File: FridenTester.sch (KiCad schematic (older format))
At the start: 16 parts, among them P1 CONN_02X05, U1 2EDN752, U2 2EDN752, U3 DG403

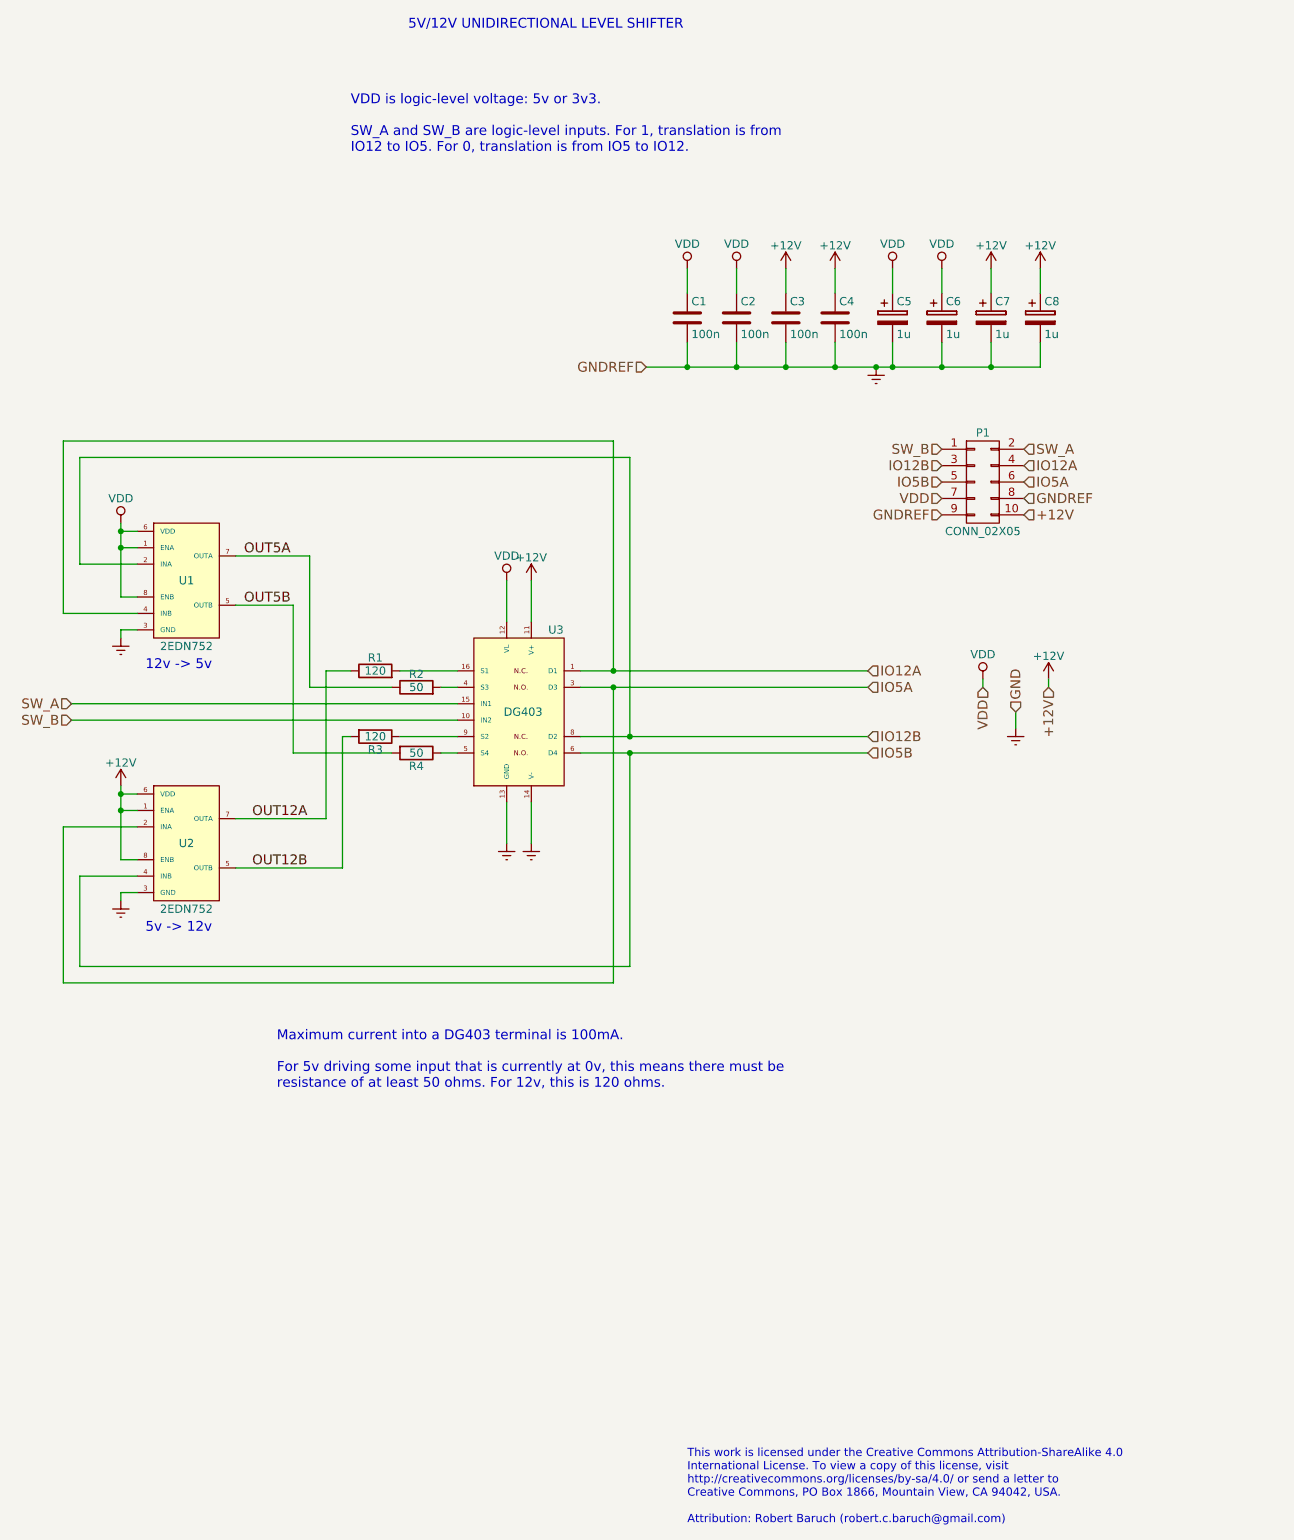
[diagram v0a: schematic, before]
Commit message: Start on rev D, with protection Schottkys
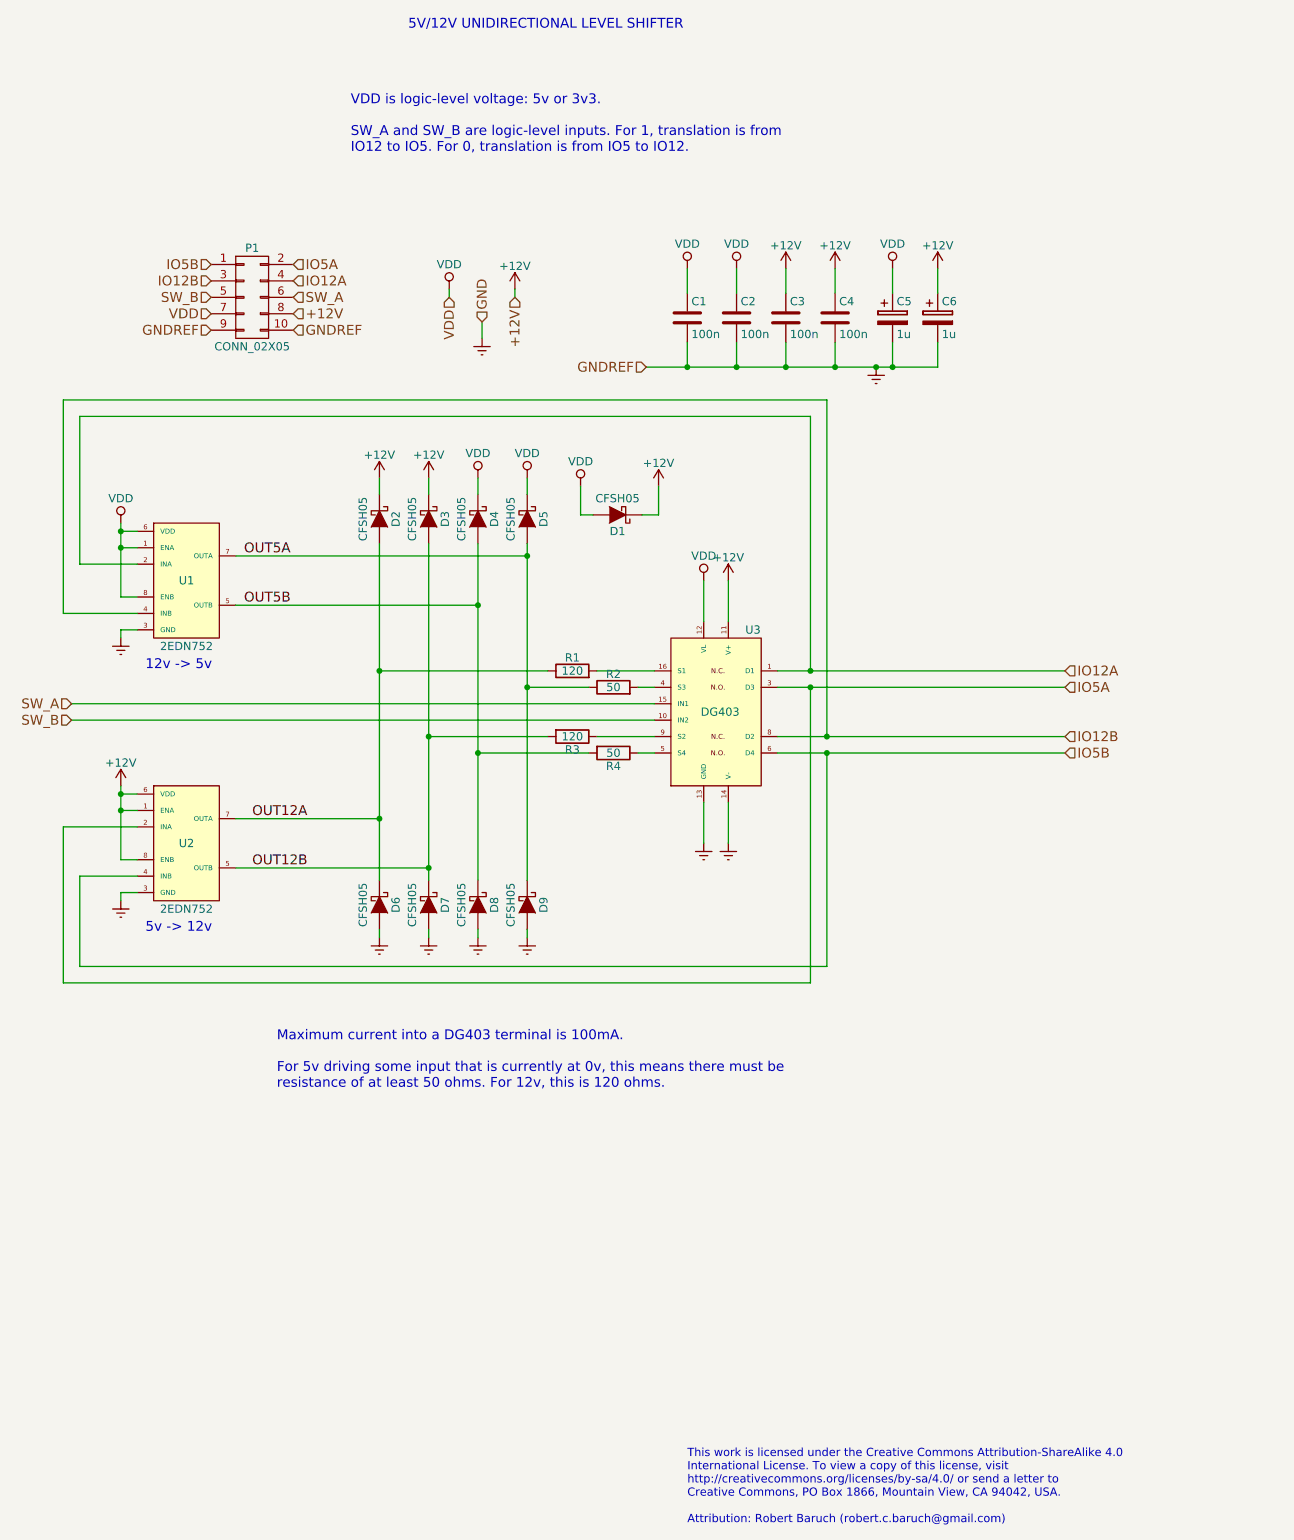
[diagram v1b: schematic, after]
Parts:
- removed C6, C8: 1u, Capacitors_SMD:C_1206, symbol CP
- added D1, D2, D3, D4, D5, D6, D7, D8, D9: CFSH05, friden-footprints:SOD-882L, symbol CFSH05
- C1, C2, C3, C4: footprint Capacitors_SMD:C_1206 -> Capacitors_SMD:C_0805
- renumbered C7 to C6
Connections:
- net +12V: now also P1.8 (P8), D1.1 (K), D2.1 (K), D3.1 (K); no longer P1.10 (P10)
- net GNDREF: now also P1.10 (P10), D6.2 (A), D7.2 (A), D8.2 (A), D9.2 (A); no longer P1.8 (P8)
- net IO12A: now also U1.2 (INA); no longer U1.4 (INB)
- net IO12B: now also U1.4 (INB); no longer U1.2 (INA)
- net IO5A: now also P1.2 (P2); no longer P1.6 (P6)
- net IO5B: now also P1.1 (P1); no longer P1.5 (P5)
- net OUT12A: now also D2.2 (A), D6.1 (K)
- net OUT12B: now also D3.2 (A), D7.1 (K)
- net OUT5A: now also D5.2 (A), D9.1 (K)
- net OUT5B: now also D4.2 (A), D8.1 (K)
- net SW_A: now also P1.6 (P6); no longer P1.2 (P2)
- net SW_B: now also P1.5 (P5); no longer P1.1 (P1)
- net VDD: now also D1.2 (A), D4.1 (K), D5.1 (K)
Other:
- moved on the sheet: C6, P1, R1, R2, R3, R4, U3
